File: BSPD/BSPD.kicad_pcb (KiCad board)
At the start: 2 copper layers, 60 x 55 mm, 111 parts, among them J2 Conn_02x10_Odd_Even, U1 TLV2371DBV, U10 TLV2371DBV, U11 TLV2371DBV, U12 74LVC1G08, U13 74LVC1G08, U14 TLV2371DBV, U15 74LVC1G08, U17 74LVC1G08, U18 74LVC1G08, U2 TLV2371DBV, U3 TLV2371DBV, U4 TLV2371DBV, U5 74LVC1G08, U6 74LVC1G08, U7 AP2204K-ADJ, U8 TLV2371DBV, U9 TLV2371DBV

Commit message: finish v2025.5
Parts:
- removed C15: 0.1u, Capacitor_SMD:C_0603_1608Metric
- removed TP13, TP14, TP17, TP18: TestPoint, TestPoint:TestPoint_THTPad_D1.5mm_Drill0.7mm
- added G***: LOGO, logo:nckufs_logo_10mm, F.Cu at (156.6, 105.2)
- added G***: LOGO, logo:galaxy_logo_10mm, F.Cu at (156.8, 110.8)
- added G***: LOGO, logo:fire_shark_logo_20mm, B.Cu at (142.0, 93.5)
- added G***: LOGO, logo:nckufs_logo_10mm, B.Cu at (154.5, 75.0)
- added kibuzzard-681DF708: G***, kibuzzard-681DF708, F.Cu at (175.0, 122.8)
- added kibuzzard-681DF91B: G***, kibuzzard-681DF91B, F.Cu at (158.8, 91.0)
- added kibuzzard-681DF939: G***, kibuzzard-681DF939, F.Cu at (160.4, 82.0)
- added kibuzzard-681DF95E: G***, kibuzzard-681DF95E, F.Cu at (139.2, 77.2)
- added kibuzzard-681DF96B: G***, kibuzzard-681DF96B, F.Cu at (137.2, 111.8)
- added kibuzzard-681DFA90: G***, kibuzzard-681DFA90, F.Cu at (151.4, 114.6)
- added kibuzzard-681DFAB1: G***, kibuzzard-681DFAB1, F.Cu at (167.4, 110.8)
- added kibuzzard-681DFABC: G***, kibuzzard-681DFABC, F.Cu at (173.2, 110.8)
- added kibuzzard-681DFAC8: G***, kibuzzard-681DFAC8, F.Cu at (145.6, 116.6)
- added kibuzzard-681DFAF7: G***, kibuzzard-681DFAF7, F.Cu at (182.8, 77.8)
- added kibuzzard-681DFB04: G***, kibuzzard-681DFB04, F.Cu at (183.2, 91.8)
- added kibuzzard-681DFC5A: G***, kibuzzard-681DFC5A, F.Cu at (186.0, 115.5)
- added kibuzzard-681DFC99: G***, kibuzzard-681DFC99, B.Cu at (143.5, 74.5)
- C13, C17, C2, C3, C4, C5, C7, D18, D7, R10, R11, R13, R19, R22, R29, R4, R5, R6, R8, TP10, TP9, U17, U3, U4, U6, U8, U9: moved to B.Cu
- R12, R28: footprint Resistor_SMD:R_0201_0603Metric -> Resistor_SMD:R_0603_1608Metric
- R25, R26: moved to F.Cu
- moved RV3 170.6 mm to (185.4, 95.6)
- moved RV4 170.6 mm to (185.4, 102.0)
- moved RV6 169.4 mm to (185.4, 108.6)
- moved U9 149.9 mm to (171.4, 108.0)
- moved U4 149.8 mm to (171.6, 103.2), turned to -90 degrees
- moved U3 148.6 mm to (171.6, 96.2), turned to -90 degrees
- moved C13 145.6 mm to (173.4, 110.8)
- moved R6 138.3 mm to (175.6, 104.4), turned to 180 degrees
- moved C4 138.1 mm to (164.6, 104.8), turned to 90 degrees
- moved C16 137.8 mm to (170.6, 103.4), turned to 90 degrees
- moved R4 136.7 mm to (175.6, 93.4), turned to 180 degrees
- moved D6 136.1 mm to (167.4, 105.6), turned to -90 degrees
- moved R5 135.6 mm to (173.4, 99.6), turned to 180 degrees
- moved C17 135.5 mm to (170.0, 99.6), turned to 180 degrees
- moved U6 135.3 mm to (164.0, 94.4), turned to 180 degrees
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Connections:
- C21 pad 2: BSE_R_Fault -> BSE_L_Fault
- D1 pad 1: APPS_Fault -> current_Fault
- D2 pad 1: BSE_L_Fault -> BSE_R_Fault
- J2 pad 10: BSE_L_Fault -> BSE_R_Fault
- J2 pad 14: BSE_R_Fault -> current_Fault
- J2 pad 16: BSPD -> Both
- J2 pad 17: BSE_R_init -> unconnected-(J2-Pin_17-Pad17)
- J2 pad 18: unconnected-(J2-Pin_18-Pad18) -> BSPD
- J2 pad 19: BSE_L_init -> current_init
- J2 pad 2: VDC -> BSE_L_init
- J2 pad 20: current_init -> BSPD
- J2 pad 3: unconnected-(J2-Pin_3-Pad3) -> VDC
- J2 pad 4: unconnected-(J2-Pin_4-Pad4) -> BSE_R_init
- J2 pad 6: Both -> BSE_L_Fault
- J2 pad 8: current_init -> unconnected-(J2-Pin_8-Pad8)
- R21 pad 1: BSE_R -> BSE_L
- R30 pad 2: BSE_R_Fault -> BSE_L_Fault
- R5 pad 1: BSE_L -> BSE_R
- U15 pad 1: Both -> current_Fault
- U15 pad 2: APPS_Fault -> Both
- U5 pad 4: APPS_Fault -> current_Fault
- U6 pad 4: BSE_L_Fault -> BSE_R_Fault
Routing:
- net +5V: track 0.00 -> 318.1 mm, vias 0 -> 10
- net BSE_L_Fault: track 0.00 -> 99.1 mm, vias 0 -> 3
- net current: track 0.00 -> 49.8 mm, vias 0 -> 3
- net current_Fault: track 0.00 -> 48.3 mm, vias 0 -> 2
- net Both: track 0.00 -> 41.2 mm, vias 0 -> 4
- net BSE_R_Fault: track 0.00 -> 40.0 mm, vias 0 -> 2
- net BSE_L: track 0.00 -> 38.6 mm, vias 0 -> 1
- net BSE_R: track 0.00 -> 27.2 mm, vias 0 -> 3
- net Net-(U18-Pad2): track 0.00 -> 27.0 mm, vias 0 -> 1
- net BSPD: track 0.00 -> 23.0 mm
- net Net-(R28-Pad2): track 0.00 -> 19.0 mm, vias 0 -> 1
- net VDC: track 0.00 -> 15.8 mm
- net Net-(U9--): track 0.00 -> 12.3 mm
- net Net-(U8--): track 0.00 -> 12.0 mm
- net Net-(R18-Pad1): track 0.00 -> 11.0 mm
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- added copper zone on B.Cu, net GND
- added copper zone on F.Cu, net GND

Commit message: v2025.07
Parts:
- removed C18, C19, C20: 0.1u, Capacitor_SMD:C_0603_1608Metric
- removed U10, U11, U14: TLV2371DBV, Package_TO_SOT_SMD:SOT-23-5
- removed kibuzzard-681DFC99: G***, kibuzzard-681DFC99
- added C15: 10u, Capacitor_SMD:C_0805_2012Metric, F.Cu at (155.4, 75.8)
- added D8: LED, LED_SMD:LED_0805_2012Metric_Pad1.15x1.40mm_HandSolder, F.Cu at (144.0, 122.0)
- added R31: 1k, Resistor_SMD:R_0603_1608Metric, F.Cu at (145.6, 118.8)
- added kibuzzard-688B2CB5: G***, kibuzzard-688B2CB5, F.Cu at (140.4, 123.8)
- added kibuzzard-688B2EEF: G***, kibuzzard-688B2EEF, B.Cu at (143.5, 74.5)
- C11: value 0.1u -> 10u; footprint Capacitor_SMD:C_0603_1608Metric -> Capacitor_SMD:C_0805_2012Metric; moved to F.Cu
- C14, R7, R9: moved to B.Cu
- C16: value 0.1u -> 10u; footprint Capacitor_SMD:C_0603_1608Metric -> Capacitor_SMD:C_0805_2012Metric
- R14: value 866k -> 301k
- R8: value 1k -> 16k
- U1, U2: value TLV2371DBV -> ~; footprint Package_TO_SOT_SMD:SOT-23-5 -> Package_SO:SO-8_3.9x4.9mm_P1.27mm
- U3: value TLV2371DBV -> ~; footprint Package_TO_SOT_SMD:SOT-23-5 -> Package_SO:SO-8_3.9x4.9mm_P1.27mm; moved to F.Cu
- U4, U8: value TLV2371DBV -> AS331KTR
- U5: value 74LVC1G08 -> 74LVC1G08QW5-7
- U9: value TLV2371DBV -> AS331KTR; moved to F.Cu
- moved C17 35.3 mm to (137.6, 113.6), turned to -90 degrees
- moved U4 32.7 mm to (140.4, 113.0)
- moved U9 28.2 mm to (145.4, 96.8)
- moved U8 27.6 mm to (171.2, 107.8)
- moved U2 23.6 mm to (170.2, 98.4), turned to 0 degrees
- moved U3 19.9 mm to (173.6, 76.4), turned to 0 degrees
- moved C14 13.1 mm to (144.8, 93.4), turned to 90 degrees
- moved C11 12.5 mm to (179.6, 75.6), turned to -90 degrees
- moved C16 9.51 mm to (171.8, 94.0), turned to 0 degrees
- moved R9 6.96 mm to (153.0, 78.6)
- moved R7 4.54 mm to (155.2, 76.0), turned to -90 degrees
- moved R3 4.22 mm to (148.2, 87.6)
- moved R21 4.21 mm to (177.6, 84.8)
- moved C6 4.20 mm to (158.8, 76.6), turned to 0 degrees
- moved C13 3.85 mm to (174.0, 107.0), turned to -90 degrees
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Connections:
- C5 pad 1: Net-(U10--) -> Net-(U9--)
- J2 pad 11: unconnected-(J2-Pin_11-Pad11) -> GND
- J2 pad 12: unconnected-(J2-Pin_12-Pad12) -> GND
- J2 pad 13: unconnected-(J2-Pin_13-Pad13) -> GND
- J2 pad 15: unconnected-(J2-Pin_15-Pad15) -> GND
- J2 pad 17: unconnected-(J2-Pin_17-Pad17) -> GND
- J2 pad 5: unconnected-(J2-Pin_5-Pad5) -> GND
- J2 pad 7: unconnected-(J2-Pin_7-Pad7) -> GND
- J2 pad 8: unconnected-(J2-Pin_8-Pad8) -> GND
- J2 pad 9: unconnected-(J2-Pin_9-Pad9) -> GND
- R11 pad 1: Net-(R11-Pad1) -> Net-(U2-1out)
- R13 pad 1: Net-(R13-Pad1) -> Net-(U2-2out)
- R18 pad 2: Net-(U11-+) -> Net-(U3-1+)
- R2 pad 2: Net-(U1--) -> Net-(U1-1-)
- R20 pad 1: Net-(R20-Pad1) -> Net-(U3-1out)
- R21 pad 2: Net-(U11--) -> Net-(U3-1-)
- R22 pad 2: Net-(U10--) -> Net-(U9--)
- R23 pad 1: Net-(R23-Pad1) -> Net-(U3-2out)
- R24 pad 2: Net-(U14--) -> Net-(U3-2-)
- R3 pad 2: Net-(U2--) -> Net-(U1-2-)
- R4 pad 2: Net-(U3-+) -> Net-(U2-1+)
- R5 pad 2: Net-(U3--) -> Net-(U2-1-)
- R6 pad 2: Net-(U4--) -> Net-(U2-2-)
- R9 pad 1: Net-(R9-Pad1) -> Net-(U1-2out)
- RV5 pad 2: Net-(U8--) -> Net-(U4--)
- RV6 pad 2: Net-(U9--) -> Net-(U8--)
- RV7 pad 2: Net-(U10-+) -> Net-(U9-+)
- TP5 pad 1: Net-(U8--) -> Net-(U4--)
- TP6 pad 1: Net-(U9--) -> Net-(U8--)
- TP7 pad 1: Net-(U10-+) -> Net-(U9-+)
- U1 pad 2: GND -> Net-(U1-1-)
- U1 pad 4: Net-(U1--) -> GND
- U1 pad 5: +5V -> Net-(U1-1-)
- U2 pad 1: Net-(R9-Pad1) -> Net-(U2-1out)
- U2 pad 2: GND -> Net-(U2-1-)
- U2 pad 3: Net-(U1--) -> Net-(U2-1+)
- U2 pad 4: Net-(U2--) -> GND
- U2 pad 5: +5V -> Net-(U2-1-)
- U3 pad 1: Net-(R11-Pad1) -> Net-(U3-1out)
- U3 pad 2: GND -> Net-(U3-1-)
- U3 pad 3: Net-(U3-+) -> Net-(U3-1+)
- U3 pad 4: Net-(U3--) -> GND
- U3 pad 5: +5V -> Net-(U3-1-)
- U4 pad 1: Net-(R13-Pad1) -> Net-(U4--)
- U4 pad 3: Net-(U3--) -> current
- U4 pad 4: Net-(U4--) -> Net-(U18-Pad1)
- U8 pad 1: Net-(U18-Pad1) -> Net-(U8--)
- U8 pad 3: current -> BSE_R
- U8 pad 4: Net-(U8--) -> Net-(U18-Pad2)
- U9 pad 1: Net-(U18-Pad2) -> Net-(U9--)
- U9 pad 3: BSE_R -> Net-(U9-+)
- U9 pad 4: Net-(U9--) -> Both
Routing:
- net Net-(U3-2-): track 0.00 -> 14.6 mm, vias 0 -> 1
- net Net-(U3-1-): track 0.00 -> 13.6 mm, vias 0 -> 1
- net Net-(U1-1-): track 0.00 -> 12.7 mm
- net Net-(U9-+): track 0.00 -> 11.8 mm
- net Net-(U3-2out): track 0.00 -> 11.8 mm, vias 0 -> 1
- net Net-(U10-+): track 10.1 -> 0.00 mm
- net Net-(U4--): track 2.28 -> 12.3 mm
- net Net-(U10--): track 10.0 -> 0.00 mm, vias 1 -> 0
- net +5V: track 318.1 -> 327.7 mm, vias 10 -> 5
- net Net-(U2-1+): track 0.00 -> 9.26 mm, vias 0 -> 1
- net Net-(U1-2-): track 0.00 -> 9.07 mm, vias 0 -> 1
- net Net-(U3-1+): track 0.00 -> 7.75 mm, vias 0 -> 1
- net Net-(U2-1-): track 0.00 -> 6.99 mm, vias 0 -> 1
- net Net-(U1-1out): track 2.15 -> 9.05 mm, vias 0 -> 1
- net Net-(U9--): track 12.3 -> 19.1 mm, vias 0 -> 1
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- added copper zone on F.Cu, net +5V

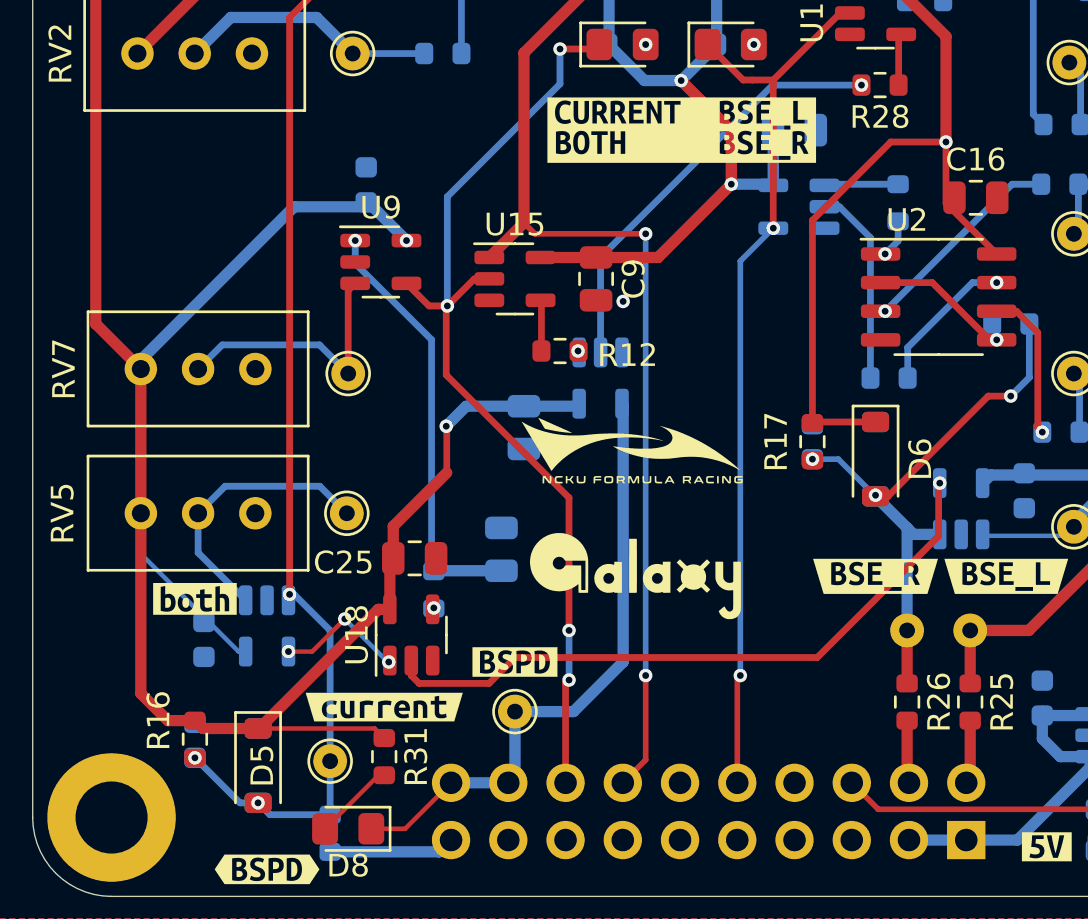
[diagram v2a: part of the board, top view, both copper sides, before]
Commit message: modify LM2903QS-13
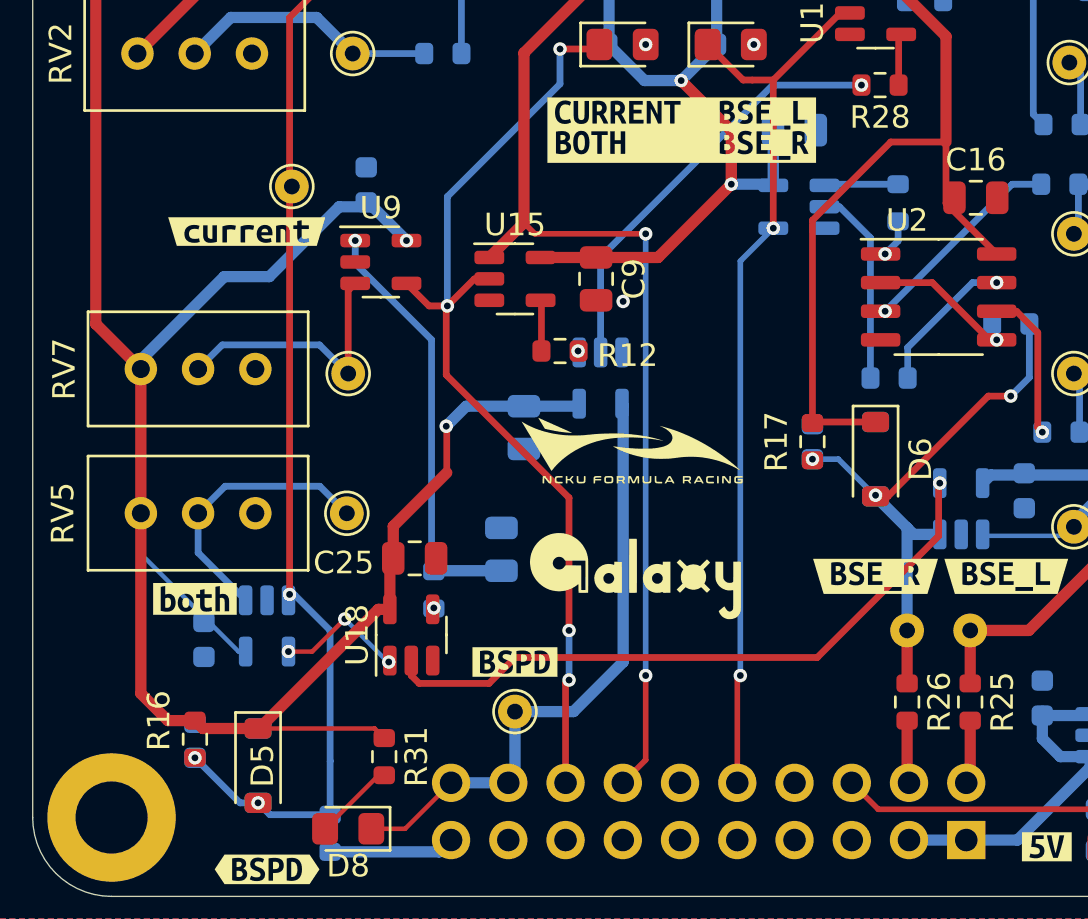
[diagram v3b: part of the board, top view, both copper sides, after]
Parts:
- removed kibuzzard-688B2EEF: G***, kibuzzard-688B2EEF
- added kibuzzard-688F84AA: G***, kibuzzard-688F84AA, B.Cu at (144.2, 73.0)
- moved TP11 25.6 mm to (141.5, 93.5)
- moved kibuzzard-681DFAC8 22.0 mm to (139.5, 95.5)
- moved G*** 2.12 mm to (156.2, 72.8)
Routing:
- net +5V: vias 5 -> 4

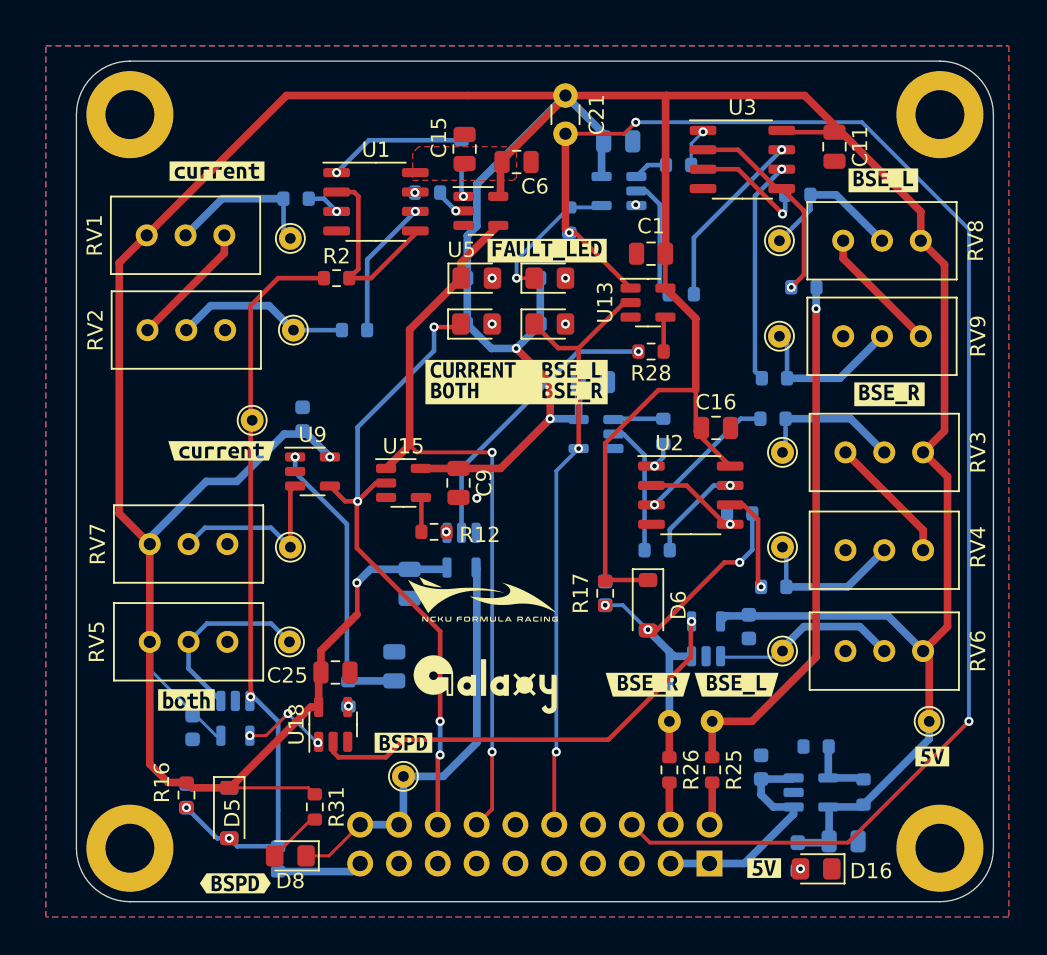
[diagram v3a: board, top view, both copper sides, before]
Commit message: fix:add pull up resistors to comparators
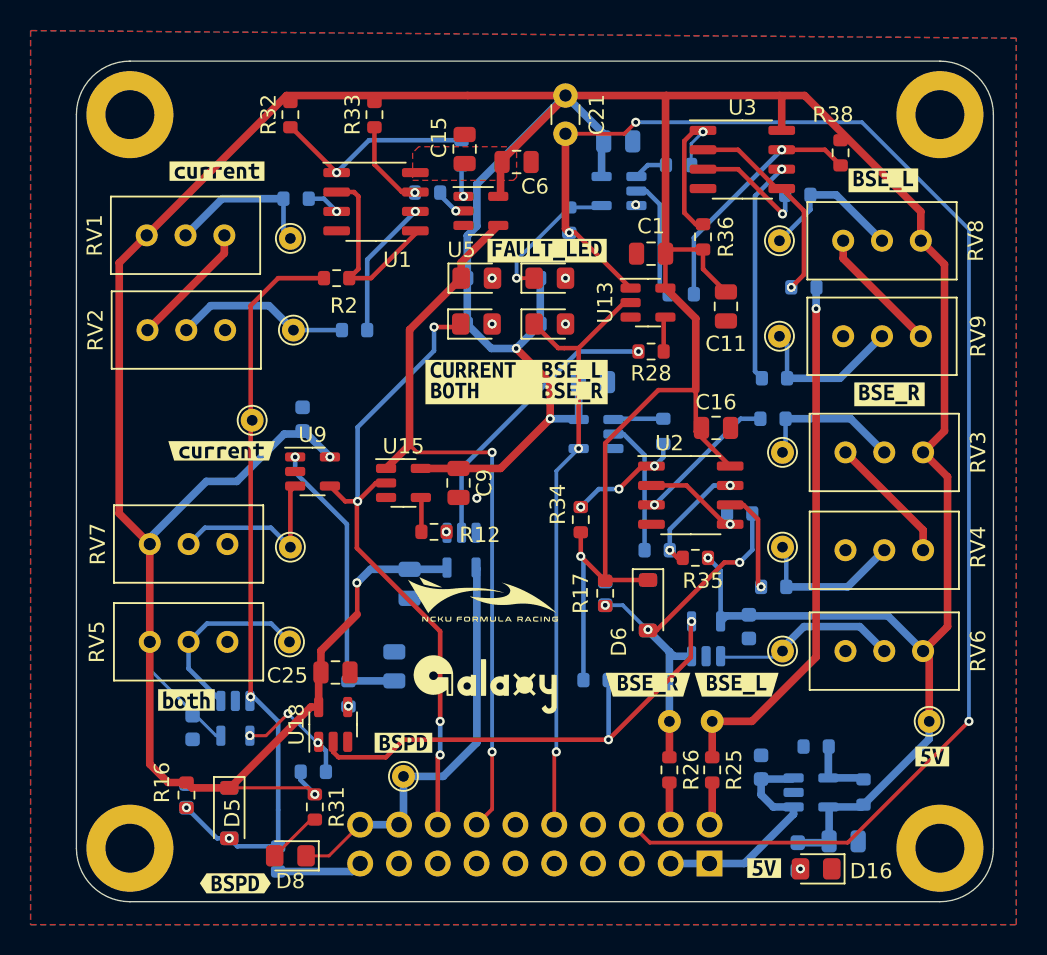
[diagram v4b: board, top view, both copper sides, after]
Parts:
- removed kibuzzard-688F84AA: G***, kibuzzard-688F84AA
- added R32: 10k, Resistor_SMD:R_0603_1608Metric, F.Cu at (144.0, 73.5)
- added R33: 10k, Resistor_SMD:R_0603_1608Metric, F.Cu at (149.5, 73.5)
- added R34: 10k, Resistor_SMD:R_0603_1608Metric, F.Cu at (163.0, 100.0)
- added R35: 10k, Resistor_SMD:R_0603_1608Metric, F.Cu at (170.5, 102.5)
- added R36: 10k, Resistor_SMD:R_0603_1608Metric, F.Cu at (171.0, 81.5)
- added R38: 10k, Resistor_SMD:R_0603_1608Metric, F.Cu at (180.0, 76.0)
- added R39: 10k, Resistor_SMD:R_0603_1608Metric, B.Cu at (145.5, 116.5)
- added R40: 10k, Resistor_SMD:R_0603_1608Metric, B.Cu at (164.0, 110.5)
- added kibuzzard-68E66274: G***, kibuzzard-68E66274, B.Cu at (144.0, 73.0)
- U2: value ~ -> LM2903QS-13
- moved C11 12.6 mm to (172.5, 86.0)
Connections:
- J2 pad 12: GND -> unconnected-(J2-Pin_12-Pad12)
- J2 pad 8: GND -> unconnected-(J2-Pin_8-Pad8)
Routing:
- net +5V: track 327.7 -> 351.0 mm, vias 4 -> 7
- net Net-(U3-1out): track 2.50 -> 10.2 mm
- net Net-(U1-2out): track 0.05 -> 5.91 mm
- net Net-(U2-1out): track 1.70 -> 7.44 mm, vias 1 -> 3
- net Net-(U3-2out): track 11.8 -> 16.1 mm
- net Net-(U1-1out): track 9.05 -> 13.3 mm
- net Net-(R40-Pad1): track 29.3 -> 33.2 mm, vias 1 -> 2
- net Net-(R39-Pad1): track 5.84 -> 7.96 mm
- net Net-(U2-2out): track 6.59 -> 7.64 mm, vias 1 -> 2
